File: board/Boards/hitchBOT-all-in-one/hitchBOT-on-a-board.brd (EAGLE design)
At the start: 100 x 55 mm, 40 parts, among them J1 22-27-2021-02, J2 22-27-2021-02, J3 22-27-2021-02, Q1 SPD30P06PTO252, Q2 SPD30P06PTO252, Q3 SPD30P06PTO252

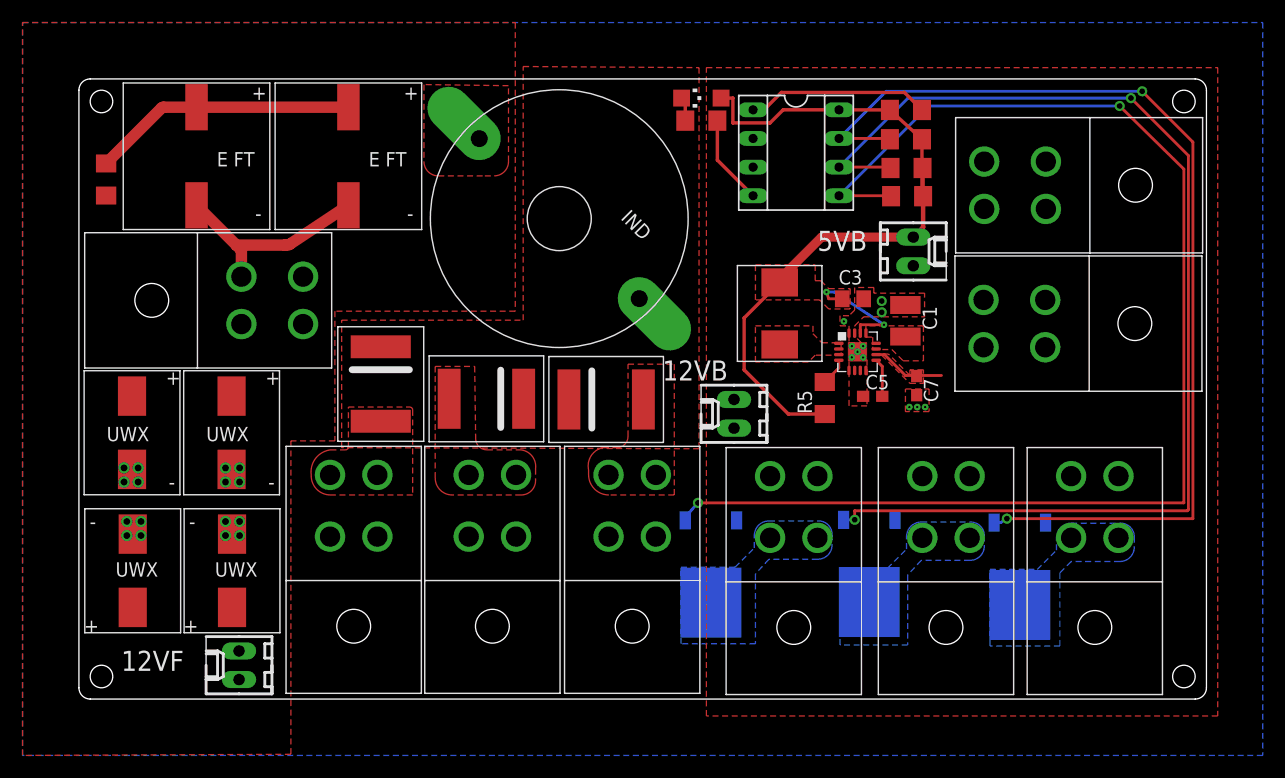
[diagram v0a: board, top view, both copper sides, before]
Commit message: modified board holes around edges
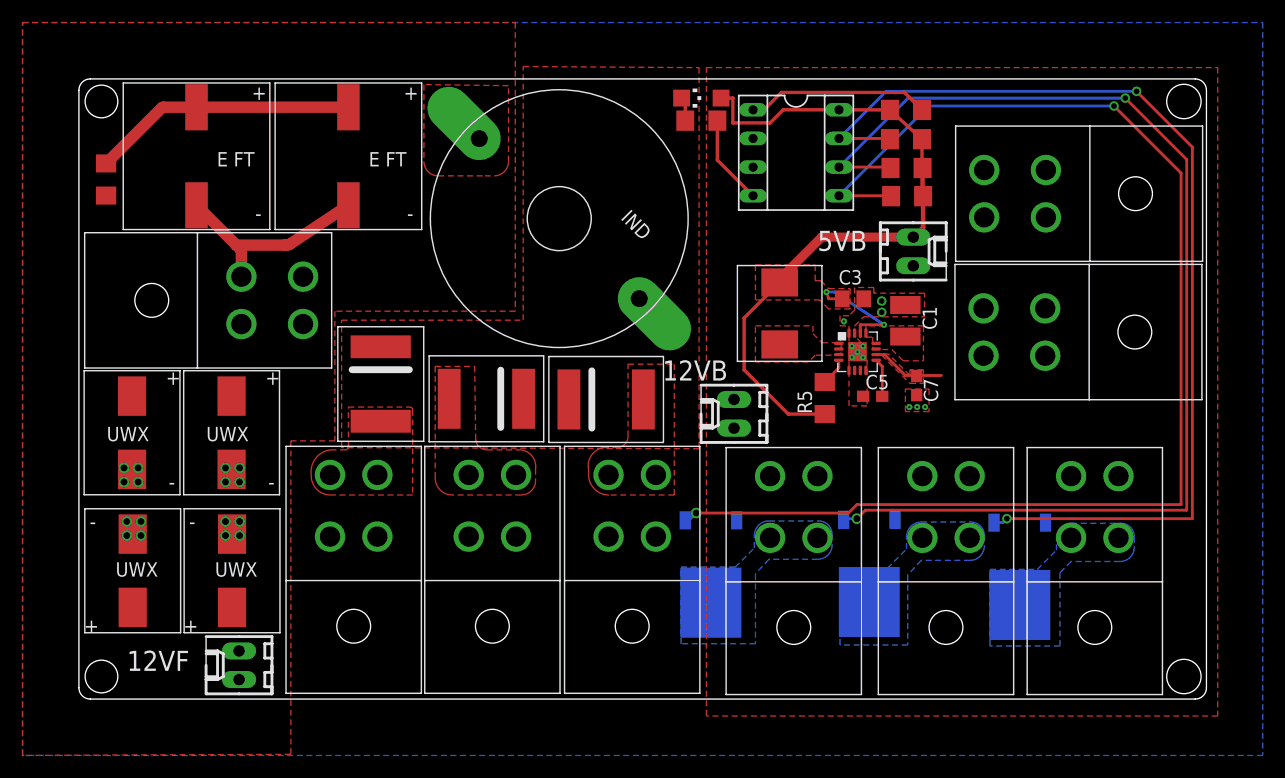
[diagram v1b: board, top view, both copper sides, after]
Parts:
- moved U$11 0.75 mm to (83.7, 44.8)
- moved U$16 0.75 mm to (83.6, 32.5)
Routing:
- net N$19: track 103.1 -> 102.1 mm
- net N$13: track 115.4 -> 114.7 mm

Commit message: finalized board, what was ordered
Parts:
- removed U$16: 2X2-MOLEX, Molex:2X2MOLEX
- added J4, J5: 22-27-2021-02, con-molex:6410-02
- moved Q1 44.0 mm to (92.8, 35.1), turned to 270 degrees
- moved U$13 24.1 mm to (83.7, 29.3), turned to 90 degrees
- moved J3 22.6 mm to (64.2, 3.50), turned to 0 degrees
- moved C13 19.9 mm to (28.1, 37.2), turned to 90 degrees
- moved Q2 13.3 mm to (95.5, 16.4), flipped to the top
- moved J1 12.7 mm to (79.3, 51.2), turned to 180 degrees
- moved Q3 10.4 mm to (61.0, 16.1), flipped to the top, turned to 270 degrees
- moved C11 7.81 mm to (12.4, 24.9), turned to 270 degrees
- moved U$12 4.70 mm to (85.4, 16.4)
- moved U$17 3.70 mm to (73.2, 16.4)
- moved C12 3.50 mm to (13.7, 14.9)
- moved C14 3.50 mm to (4.87, 14.9)
- moved R1 3.47 mm to (5.41, 44.3)
- moved U$11 3.30 mm to (83.7, 41.5)
- moved U$1 3.25 mm to (13.7, 48.1)
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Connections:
- net GND: now also J4.1, J5.1; no longer U$16.GNDL, U$16.GNDR
- net N$8: now also J4.2, J5.2; no longer U$16.POWERL, U$16.POWERR
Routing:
- net N$13: track 114.7 -> 49.5 mm, vias 2 -> 0
- net N$19: track 102.1 -> 38.0 mm, vias 2 -> 0
- net N$11: track 90.3 -> 67.0 mm, vias 2 -> 1
- net N$15: track 72.8 -> 82.7 mm
- net N$20: track 2.33 -> 4.47 mm
- net GND: track 29.3 -> 27.9 mm, vias 27 -> 28
- net N$2: track 23.5 -> 24.5 mm
- added copper zone on layer 1, net N$10
- added copper zone on layer 1, net N$18
- removed copper zone on layer 16, net N$10
- removed copper zone on layer 16, net N$18
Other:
- board text removed: "UNSWITCHED 12V"
